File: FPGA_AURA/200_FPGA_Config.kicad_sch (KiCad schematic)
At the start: 3 parts, among them U1 XC7A35T-2FTG256C, U2 W25Q256JVEIQ, U3 FT232HQ-REEL

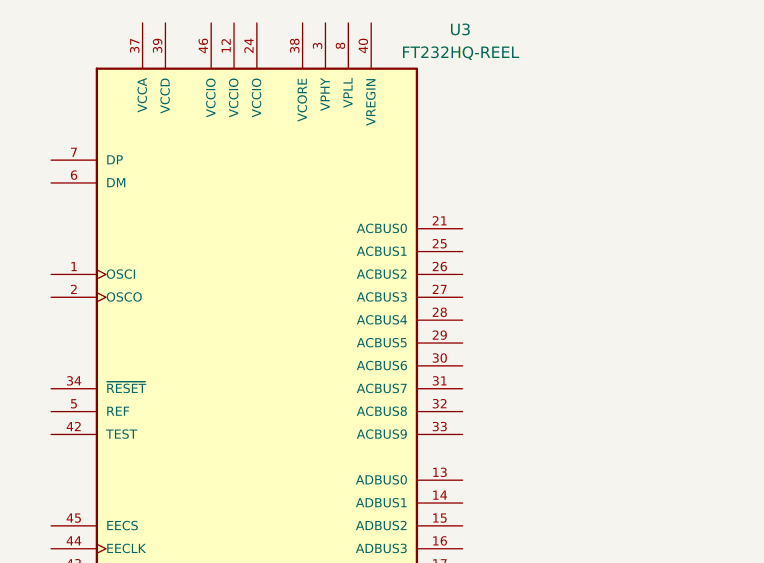
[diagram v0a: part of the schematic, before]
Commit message: Added USB power schottky and started DDR3L
Transferring from laptop to PC to decide DDR3 pins.
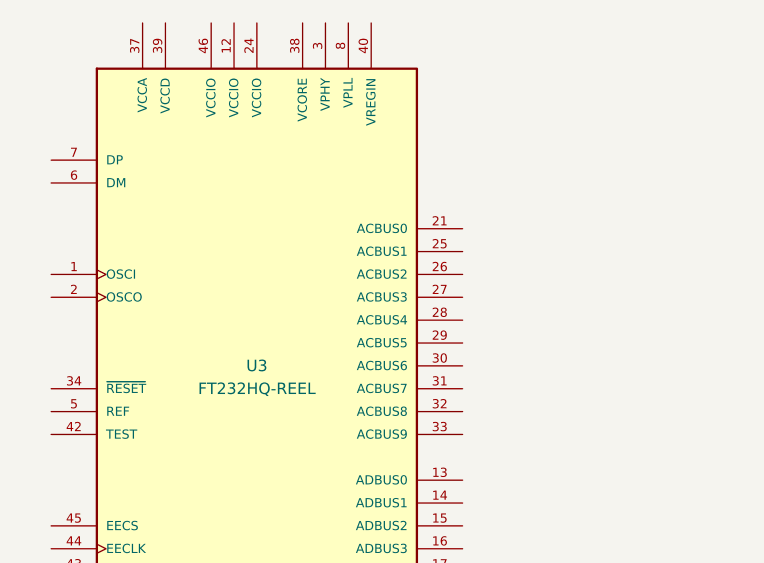
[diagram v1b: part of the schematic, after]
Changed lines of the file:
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@@
 		(dnp no)
 		(property "Reference" "U3"
-			(at 93.726 49.022 0)
+			(at 71.12 86.36 0)
 			(effects
 				(font
@@
 		)
 		(property "Value" "FT232HQ-REEL"
-			(at 93.726 51.562 0)
+			(at 71.12 88.9 0)
 			(effects
 				(font

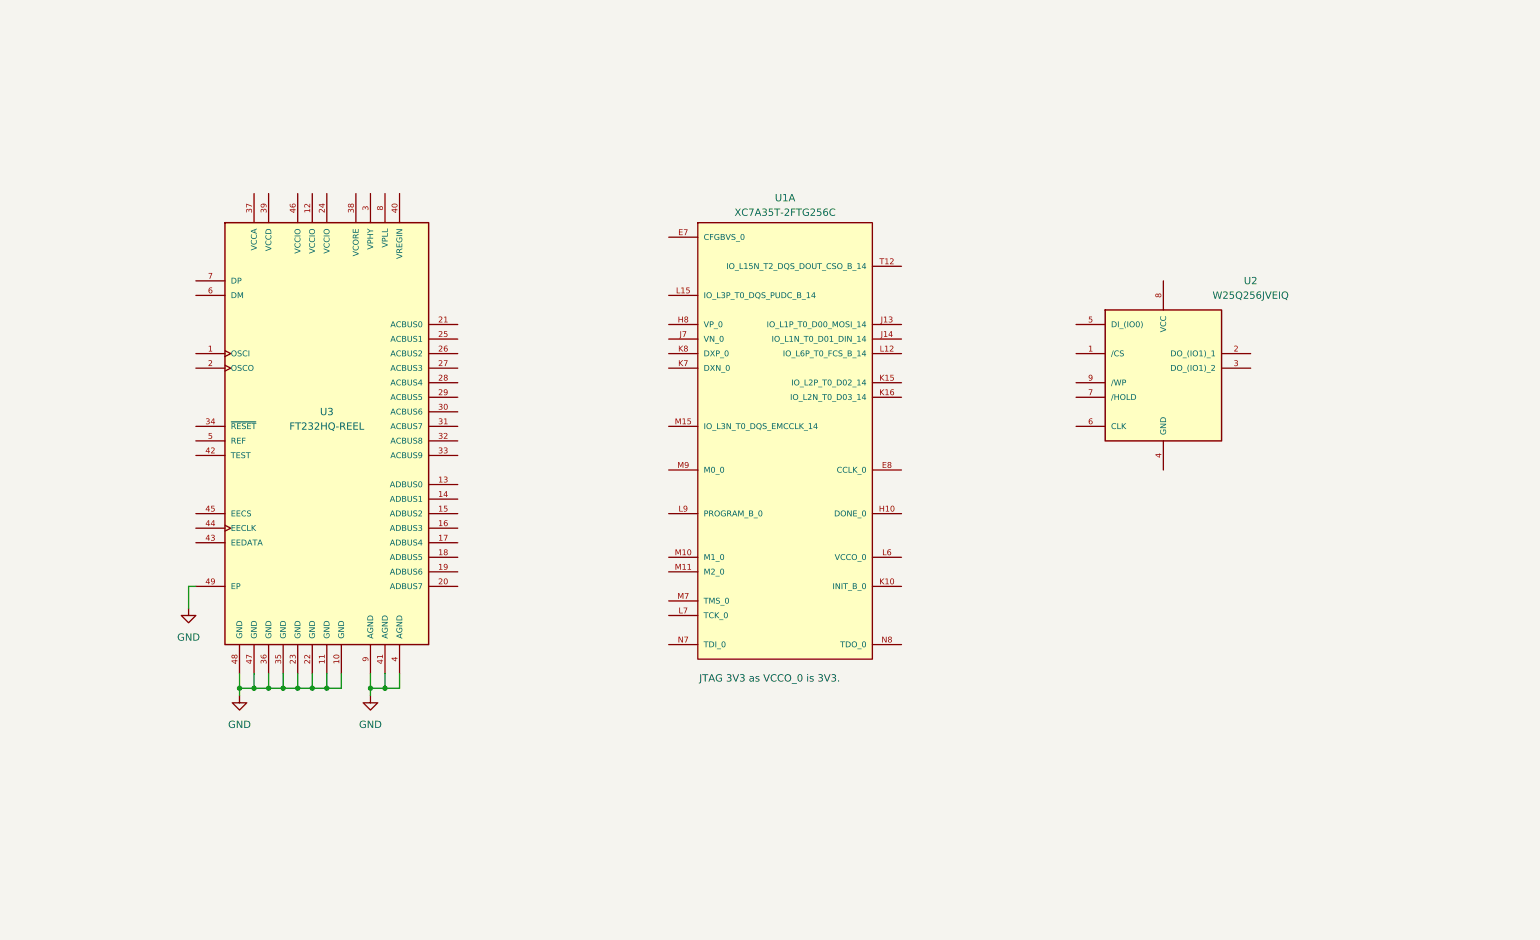
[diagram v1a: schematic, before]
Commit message: Added Connectors, FPGA Power and organized sheets.
All schematic sheets now go up in order with the correct prefix.
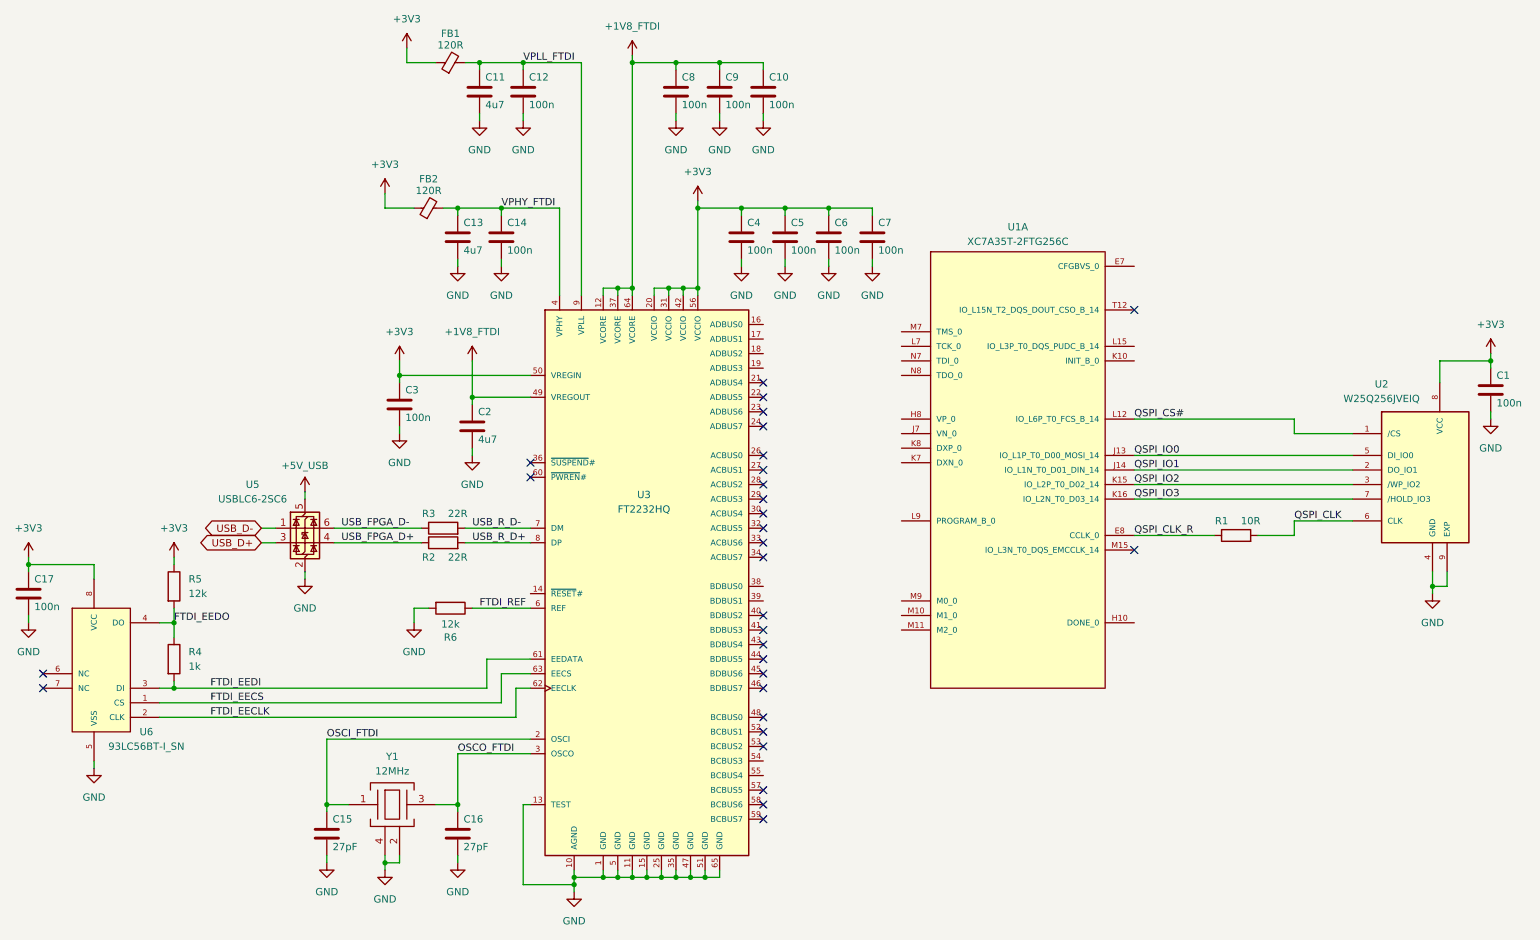
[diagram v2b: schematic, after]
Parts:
- removed U3: FT232HQ-REEL, FT232HQ-REEL:QFN50P800X800X90-49N, symbol FT232HQ-REEL:FT232HQ-REEL
- added C1, C10, C12, C14, C17, C3, C4, C5, C6, C7, C8, C9: 100n, Capacitor_SMD:C_0402_1005Metric, symbol Device:C
- added C11, C13, C2: 4u7, Capacitor_SMD:C_0402_1005Metric, symbol Device:C
- added C15, C16: 27pF, Capacitor_SMD:C_0402_1005Metric, symbol Device:C
- added FB1, FB2: 120R, Inductor_SMD:L_0603_1608Metric, symbol Device:FerriteBead_Small
- added R1: 10R, Resistor_SMD:R_0402_1005Metric, symbol Device:R
- added R2, R3: 22R, Resistor_SMD:R_0402_1005Metric, symbol Device:R
- added R4: 1k, Resistor_SMD:R_0402_1005Metric, symbol Device:R
- added R5, R6: 12k, Resistor_SMD:R_0402_1005Metric, symbol Device:R
- added U3: FT2232HQ, FT2232HQ:QFN50P900X900X100-65N, symbol FT2232HQ:FT2232HQ
- added U5: USBLC6-2SC6, Package_TO_SOT_SMD:SOT-23-6, symbol Power_Protection:USBLC6-2SC6
- added U6: 93LC56BT-I_SN, 93LC56BT-I_SN:SOIC127P600X175-8N, symbol 93LC56BT-I_SN:93LC56BT-I_SN
- added Y1: 12MHz, X322512MSB4SI:X322512MSB4SI, symbol X322512MSB4SI:X322512MSB4SI
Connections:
- net GND: now also U2.4 (GND), U2.9 (EXP), C1.2, C10.2, C11.2, C12.2, C13.2, C14.2, C15.2, C16.2, C17.2, C2.2, C3.2, C4.2, C5.2, C6.2, C7.2, C8.2, C9.2, R6.2, U3.1 (GND), U3.10 (AGND), U3.11 (GND), U3.13 (TEST), U3.15 (GND), U3.25 (GND), U3.35 (GND), U3.47 (GND), U3.5 (GND), U3.51 (GND), U3.65 (GND), U5.2 (GND), U6.5 (VSS), Y1.2, Y1.4
- net QSPI_CS#: now reaches U2.1 (/CS)
- net QSPI_CS#: now also U1.L12 (IO_L6P_T0_FCS_B_14)
- net QSPI_IO1: now reaches U2.2 (DO_IO1)
- net QSPI_IO1: now also U1.J14 (IO_L1N_T0_D01_DIN_14)
- net QSPI_IO2: now reaches U2.3 (/WP_IO2)
- net QSPI_IO2: now also U1.K15 (IO_L2P_T0_D02_14)
- net QSPI_IO0: now reaches U2.5 (DI_IO0)
- net QSPI_IO0: now also U1.J13 (IO_L1P_T0_D00_MOSI_14)
- net QSPI_CLK: now reaches U2.6 (CLK)
- net QSPI_CLK: now also R1.2
- net QSPI_IO3: now reaches U2.7 (/HOLD_IO3)
- net QSPI_IO3: now also U1.K16 (IO_L2N_T0_D03_14)
- net +3V3: now reaches U2.8 (VCC)
- net +3V3: now also C1.1, C17.1, C3.1, C4.1, C5.1, C6.1, C7.1, FB1.1, FB2.1, R5.1, U3.20 (VCCIO), U3.31 (VCCIO), U3.42 (VCCIO), U3.50 (VREGIN), U3.56 (VCCIO), U6.8 (VCC)
- net QSPI_CLK_R: now reaches U1.E8 (CCLK_0)
- net QSPI_CLK_R: now also R1.1
- new net +1V8_FTDI: C10.1, C2.1, C8.1, C9.1, U3.12 (VCORE), U3.37 (VCORE), U3.49 (VREGOUT), U3.64 (VCORE)
- new net +5V_USB: U5.5 (VBUS)
- new net FTDI_EECLK: U3.62 (EECLK), U6.2 (CLK)
- new net FTDI_EECS: U3.63 (EECS), U6.1 (CS)
- new net FTDI_EEDI: R4.2, U3.61 (EEDATA), U6.3 (DI)
- new net FTDI_EEDO: R4.1, R5.2, U6.4 (DO)
- new net FTDI_REF: R6.1, U3.6 (REF)
- new net OSCI_FTDI: C15.1, U3.2 (OSCI), Y1.1
- new net OSCO_FTDI: C16.1, U3.3 (OSCO), Y1.3
- new net USB_D+: U5.3 (I/O2)
- new net USB_D-: U5.1 (I/O1)
- new net USB_FPGA_D+: R2.1, U5.4 (I/O2)
- new net USB_FPGA_D-: R3.1, U5.6 (I/O1)
- new net USB_R_D+: R2.2, U3.8 (DP)
- new net USB_R_D-: R3.2, U3.7 (DM)
- new net VPHY_FTDI: C13.1, C14.1, FB2.2, U3.4 (VPHY)
- new net VPLL_FTDI: C11.1, C12.1, FB1.2, U3.9 (VPLL)
- no-connect marks 0 -> 30
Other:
- note removed: "JTAG 3V3 as VCCO_0 is 3V3."
- moved on the sheet: U2
